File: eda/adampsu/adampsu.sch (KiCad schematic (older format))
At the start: 15 parts, among them J1 Barrel_Jack_Switch, J2 Conn_2Rows-09Pins, J3 DB9_Female, SW1 SW_Push_SPDT, U1 LM27761, U2 LT1084-5.0

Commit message: BOM completeled but using expensive LDO
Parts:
- added PC?: PlungerCap, adampsu:PlungerCap-4JWHT, symbol Custom:PlungerCap
- added Q1: BUK7880-55A_CUX, Package_TO_SOT_SMD:SOT-223-3_TabPin2, symbol Custom:BUK7880-55A_CUX
- added R3: 1k, Resistor_SMD:R_0603_1608Metric_Pad1.05x0.95mm_HandSolder, symbol Device:R
- added R4: 10k, Resistor_SMD:R_0603_1608Metric_Pad1.05x0.95mm_HandSolder, symbol Device:R
- C1, C5, C6: footprint Capacitor_SMD:C_1206_3216Metric_Pad1.42x1.75mm_HandSolder -> Capacitor_SMD:C_0603_1608Metric_Pad1.05x0.95mm_HandSolder; symbol Device:C -> adampsu-rescue:C-Device; dk (none) -> 1276-2087-1-ND; mfr (none) -> CL10B475KQ8NQNC
- C2: symbol Device:C -> adampsu-rescue:C-Device; dk (none) -> 1276-6524-1-ND; mfr (none) -> CL10B105MO8NNWC
- C3: symbol Device:C -> adampsu-rescue:C-Device; dk (none) -> 1276-6641-1-ND; mfr (none) -> CL31B106MOHNNNE
- C4: symbol Device:C -> adampsu-rescue:C-Device; dk (none) -> 1276-2769-1-ND; mfr (none) -> CL31B226KPHNNNE
- D1: footprint Diode_SMD:D_SMB -> Diode_SMD:D_SMA-SMB_Universal_Handsoldering; symbol Diode:B240 -> adampsu-rescue:B240-Diode; dk (none) -> B240A-E3/61TGICT-ND; mfr (none) -> B240A-E3/61T
- J1: footprint Connector_BarrelJack:BarrelJack_Horizontal -> adampsu:BarrelJack_CUI_PJ-047AH_Horizontal; symbol Connector:Barrel_Jack_Switch -> adampsu-rescue:Barrel_Jack_Switch-Connector; dk (none) -> CP-047AH-ND; mfr (none) -> PJ-047AH
- J2: footprint (none) -> Connector_PinHeader_2.54mm:PinHeader_2x05_P2.54mm_Vertical; symbol Connector_Generic:Conn_2Rows-09Pins -> adampsu-rescue:Conn_2Rows-09Pins-Connector_Generic
- J3: footprint (none) -> Connector_Dsub:DSUB-9_Female_Vertical_P2.77x2.84mm_MountingHoles; symbol Connector:DB9_Female -> adampsu-rescue:DB9_Female-Connector; dk (none) -> AE10928-ND; mfr (none) -> A-DF 09 PP/Z
- R1: footprint Capacitor_SMD:C_0603_1608Metric_Pad1.05x0.95mm_HandSolder -> Resistor_SMD:R_0603_1608Metric_Pad1.05x0.95mm_HandSolder; symbol Device:R -> adampsu-rescue:R-Device; dk (none) -> 541-1.54MLCT-ND; mfr (none) -> CRCW04021M54FKED
- R2: footprint Capacitor_SMD:C_0603_1608Metric_Pad1.05x0.95mm_HandSolder -> Resistor_SMD:R_0603_1608Metric_Pad1.05x0.95mm_HandSolder; symbol Device:R -> adampsu-rescue:R-Device; dk (none) -> RMCF0603FT499KCT-ND; mfr (none) -> RMCF0603FT499K
- SW1: value SW_Push_SPDT -> 30V 300mA Latching Switch; footprint (none) -> adampsu:Switch-LC1258EENP; symbol Switch:SW_Push_SPDT -> adampsu-rescue:SW_Push_SPDT-Switch; dk (none) -> EG5886-ND; mfr (none) -> LC1258EENP
- U1: symbol Regulator_SwitchedCapacitor:LM27761 -> adampsu-rescue:LM27761-Regulator_SwitchedCapacitor; dk (none) -> 296-44379-1-ND; mfr (none) -> LM27761DSGR
- U2: symbol Regulator_Linear:LT1084-5.0 -> adampsu-rescue:LT1084-5.0-Regulator_Linear
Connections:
- net labels added: GND-F
- wire segments 35 -> 43
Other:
- note added: "12V Power in and low side switch"
- note added: "Connection to computer"
- note added: "Inductive load \nflyback diode"
- moved on the sheet: C1, C2, C3, C4, C5, C6, R1, R2

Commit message: switch to buck regulator. Need to choose parts
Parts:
- removed U2: LT1084-5.0, Package_TO_SOT_THT:TO-220-3_Vertical, symbol adampsu-rescue:LT1084-5.0-Regulator_Linear
- added C? (x2): 4.7uF, Capacitor_SMD:C_0603_1608Metric_Pad1.05x0.95mm_HandSolder, symbol adampsu-rescue:C-Device
- added C? (x2): 0.01uF, Capacitor_SMD:C_0603_1608Metric_Pad1.05x0.95mm_HandSolder, symbol adampsu-rescue:C-Device
- added C? (x2): 0.1uF, symbol Device:C
- added C? (x2): 47uF, symbol adampsu-rescue:C-Device
- added C? (x2): ?, symbol adampsu-rescue:C-Device
- added C? (x2): 2200pF, symbol Device:C
- added D?: D_Schottky, symbol Device:D_Schottky
- added L?: INDUCTOR, symbol pspice:INDUCTOR
- added R?: 665k, symbol Device:R
- added R?: 130k, symbol Device:R
- added R?: 51.1, symbol Device:R
- added R?: 10.2k, symbol Device:R
- added R?: 1.96k, symbol Device:R
- added R?: R, symbol Device:R
- added U?: TPS54531DDAR, Package_SO:TI_SO-PowerPAD-8_ThermalVias, symbol Custom:TPS54531DDAR
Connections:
- wire segments 43 -> 78
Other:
- moved on the sheet: C1, C2, C3, C4, C5, C6, D1, J2, J3, PC?, R1, R2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

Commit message: Final parts selection finished
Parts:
- removed C3: 10uF, Capacitor_SMD:C_1206_3216Metric_Pad1.42x1.75mm_HandSolder, symbol adampsu-rescue:C-Device
- removed C? (x2): ?, symbol adampsu-rescue:C-Device
- added C15: 0.01uF, Capacitor_SMD:C_0603_1608Metric_Pad1.05x0.95mm_HandSolder, symbol adampsu-rescue:C-Device
- C1, C6: footprint Capacitor_SMD:C_0603_1608Metric_Pad1.05x0.95mm_HandSolder -> Capacitor_SMD:C_1206_3216Metric_Pad1.42x1.75mm_HandSolder; dk 1276-2087-1-ND -> GRM32ER71H475KA88L; maxV (none) -> 50; mfr CL10B475KQ8NQNC -> UMK316AB7475KL-T; rating (none) -> XR7
- C10, C8: renamed from C?; dk (none) -> 399-7842-1-ND; mfr (none) -> C0603C103M5RACTU; rating (none) -> XR7
- C11: renamed from C?; footprint (none) -> Capacitor_SMD:C_0603_1608Metric_Pad1.05x0.95mm_HandSolder; dk (none) -> 399-17586-1-ND; maxV (none) -> 50; mfr (none) -> C0603C222K5RAC7411; rating (none) -> XR7
- C12: renamed from C?; value 2200pF -> 22pF; footprint (none) -> Capacitor_SMD:C_0603_1608Metric_Pad1.05x0.95mm_HandSolder; dk (none) -> 478-6204-1-ND; maxV (none) -> 50; mfr (none) -> 06035C220JAT2A; rating (none) -> XR7
- C13, C14: renamed from C?; footprint (none) -> Capacitor_SMD:C_1210_3225Metric_Pad1.42x2.65mm_HandSolder; dk (none) -> 587-5922-1-ND; maxV (none) -> 10+; mfr (none) -> LMK325B7476MM-PR; rating (none) -> XR7
- C16: renamed from C?; footprint (none) -> Capacitor_SMD:C_0603_1608Metric_Pad1.05x0.95mm_HandSolder; dk (none) -> 1276-1012-2-ND; maxV (none) -> 25; mfr (none) -> CL10F104ZB8NNNC; rating (none) -> XR7
- C2: dk 1276-6524-1-ND -> 399-11133-1-ND; maxV (none) -> 10; mfr CL10B105MO8NNWC -> C0603C105K8RACTU; rating (none) -> XR7
- C3: renamed from C?; value 4.7uF -> 100uF; footprint Capacitor_SMD:C_0603_1608Metric_Pad1.05x0.95mm_HandSolder -> Capacitor_THT:CP_Radial_D8.0mm_P3.50mm; dk 1276-2087-1-ND -> 1189-1659-1-ND; maxV (none) -> 50; mfr CL10B475KQ8NQNC -> 50YXJ100MT78X11.5; rating (none) -> XR7
- C4: value 22uF -> 4.7uF; dk 1276-2769-1-ND -> GRM32ER71H475KA88L; maxV (none) -> 50; mfr CL31B226KPHNNNE -> UMK316AB7475KL-T; rating (none) -> XR7
- C5: value 4.7uF -> 10uF; footprint Capacitor_SMD:C_0603_1608Metric_Pad1.05x0.95mm_HandSolder -> Capacitor_SMD:C_0805_2012Metric_Pad1.15x1.40mm_HandSolder; dk 1276-2087-1-ND -> 490-14381-1-ND; maxV (none) -> 10+; mfr CL10B475KQ8NQNC -> GRM21BR71A106KA73K; rating (none) -> XR7
- C7: renamed from C?; footprint Capacitor_SMD:C_0603_1608Metric_Pad1.05x0.95mm_HandSolder -> Capacitor_SMD:C_1206_3216Metric_Pad1.42x1.75mm_HandSolder; dk 1276-2087-1-ND -> GRM32ER71H475KA88L; maxV (none) -> 50; mfr CL10B475KQ8NQNC -> UMK316AB7475KL-T; rating (none) -> XR7
- C9: renamed from C?; footprint (none) -> adampsu:C_0508_1220Metric_Pad1.40x1.15mm_HandSolder; dk (none) -> 490-4346-1-ND; maxV (none) -> 25; mfr (none) -> LLL216R71E104MA01L; rating (none) -> XR7
- D1: value B240 -> D_Schottky; footprint Diode_SMD:D_SMA-SMB_Universal_Handsoldering -> Diode_SMD:D_SMC_Handsoldering; dk B240A-E3/61TGICT-ND -> 641-1126-1-ND; maxV (none) -> 40; mfr B240A-E3/61T -> CDBC540-G
- D2: renamed from D?; footprint (none) -> Diode_SMD:D_SMC_Handsoldering; dk (none) -> 641-1126-1-ND; maxV (none) -> 40; mfr (none) -> CDBC540-G
- J2: dk (none) -> 1849-1002-ND; mfr (none) -> PR20205VBDN
- L1: renamed from L?; value INDUCTOR -> 4.7uH; footprint (none) -> adampsu:L_11.5x10.3_H4.8; dk (none) -> 553-3001-1-ND; mfr (none) -> PA4342.472NLT; rating (none) -> 15.5mOhm
- R10: renamed from R?; footprint (none) -> Resistor_SMD:R_0603_1608Metric_Pad1.05x0.95mm_HandSolder; dk (none) -> 311-1.96KHRCT-ND; mfr (none) -> RC0603FR-071K96L
- R5: renamed from R?; footprint (none) -> Resistor_SMD:R_0603_1608Metric_Pad1.05x0.95mm_HandSolder; dk (none) -> 311-665KHRCT-ND; mfr (none) -> RES SMD 665K OHM 1% 1/10W 0603
- R6: renamed from R?; footprint (none) -> Resistor_SMD:R_0603_1608Metric_Pad1.05x0.95mm_HandSolder; dk (none) -> 2019-RK73B1JTTD134JCT-ND; mfr (none) -> RK73B1JTTD134J
- R7: renamed from R?; value R -> 37.4k; footprint (none) -> Resistor_SMD:R_0603_1608Metric_Pad1.05x0.95mm_HandSolder; dk (none) -> 311-37.4KHRCT-ND; mfr (none) -> RC0603FR-0737K4L
- R8: renamed from R?; footprint (none) -> Resistor_SMD:R_0603_1608Metric_Pad1.05x0.95mm_HandSolder; dk (none) -> 311-51.1HRCT-ND; mfr (none) -> RC0603FR-0751R1L
- R9: renamed from R?; footprint (none) -> Resistor_SMD:R_0603_1608Metric_Pad1.05x0.95mm_HandSolder; dk (none) -> RMCF0603FT10K2CT-ND; mfr (none) -> RMCF0603FT10K2
- U2: renamed from U?; dk (none) -> 296-40801-2-ND; mfr (none) -> TPS54531DDAR
- gave numbers to parts that had none: 1
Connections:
- net +12V: now also C4.1
- net +5V: now also C15.1
- net GND: now also C4.2, C15.2
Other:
- moved on the sheet: C1, C10, C11, C12, C13, C14, C2, C3, C5, C6, C7, C8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

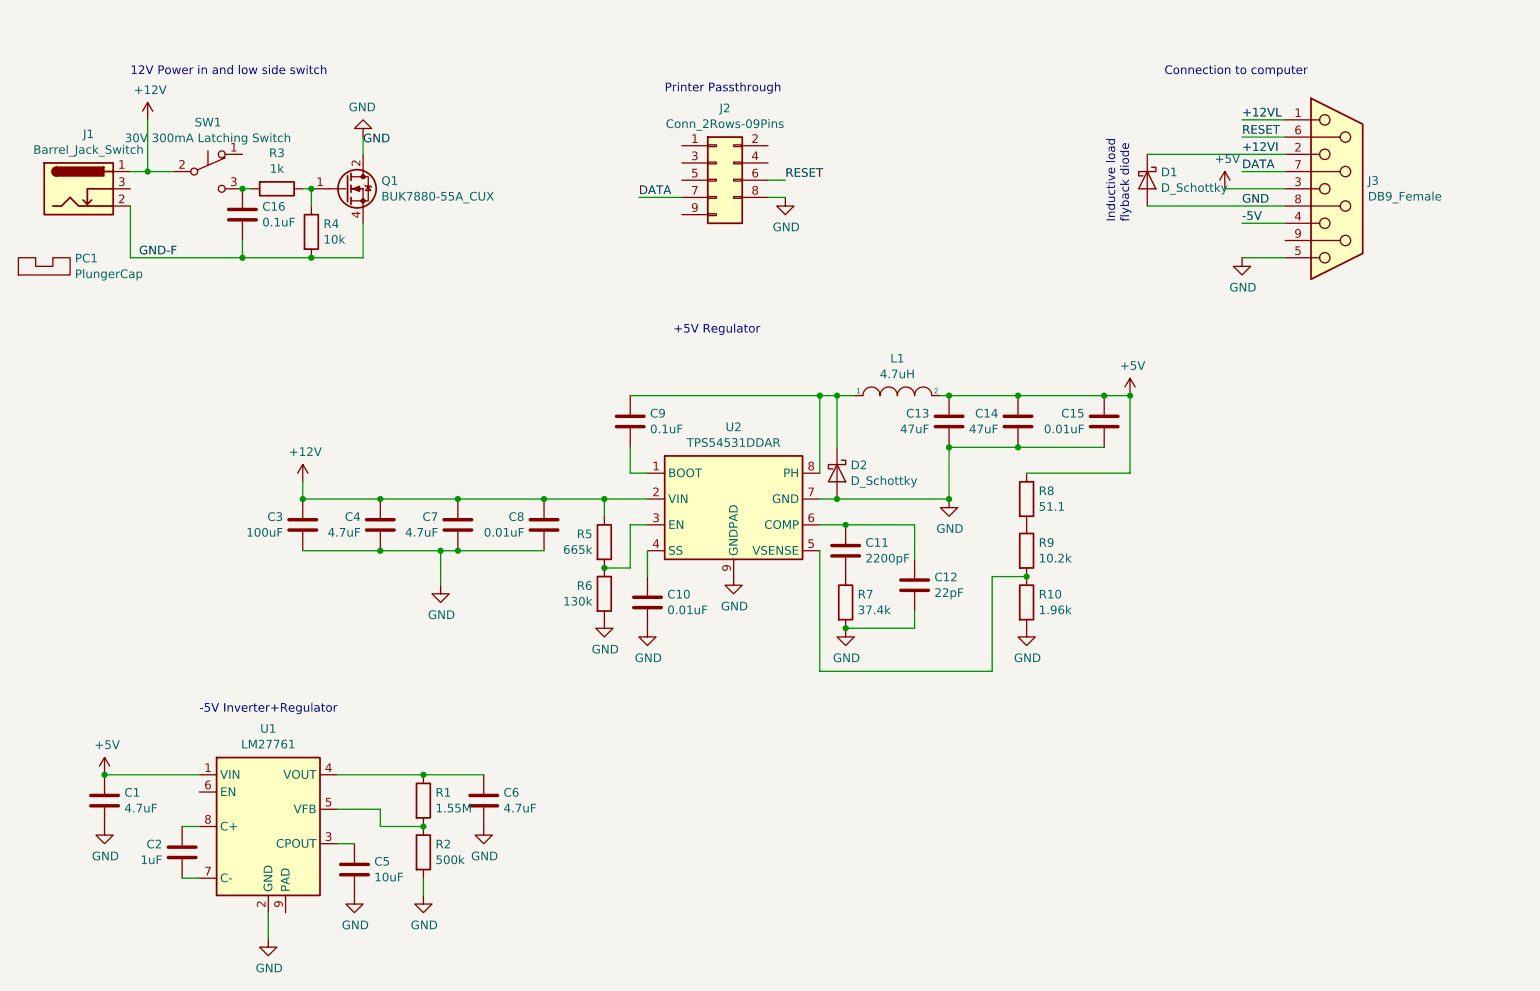
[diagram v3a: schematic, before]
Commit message: board layout started, but need new -5V regulator
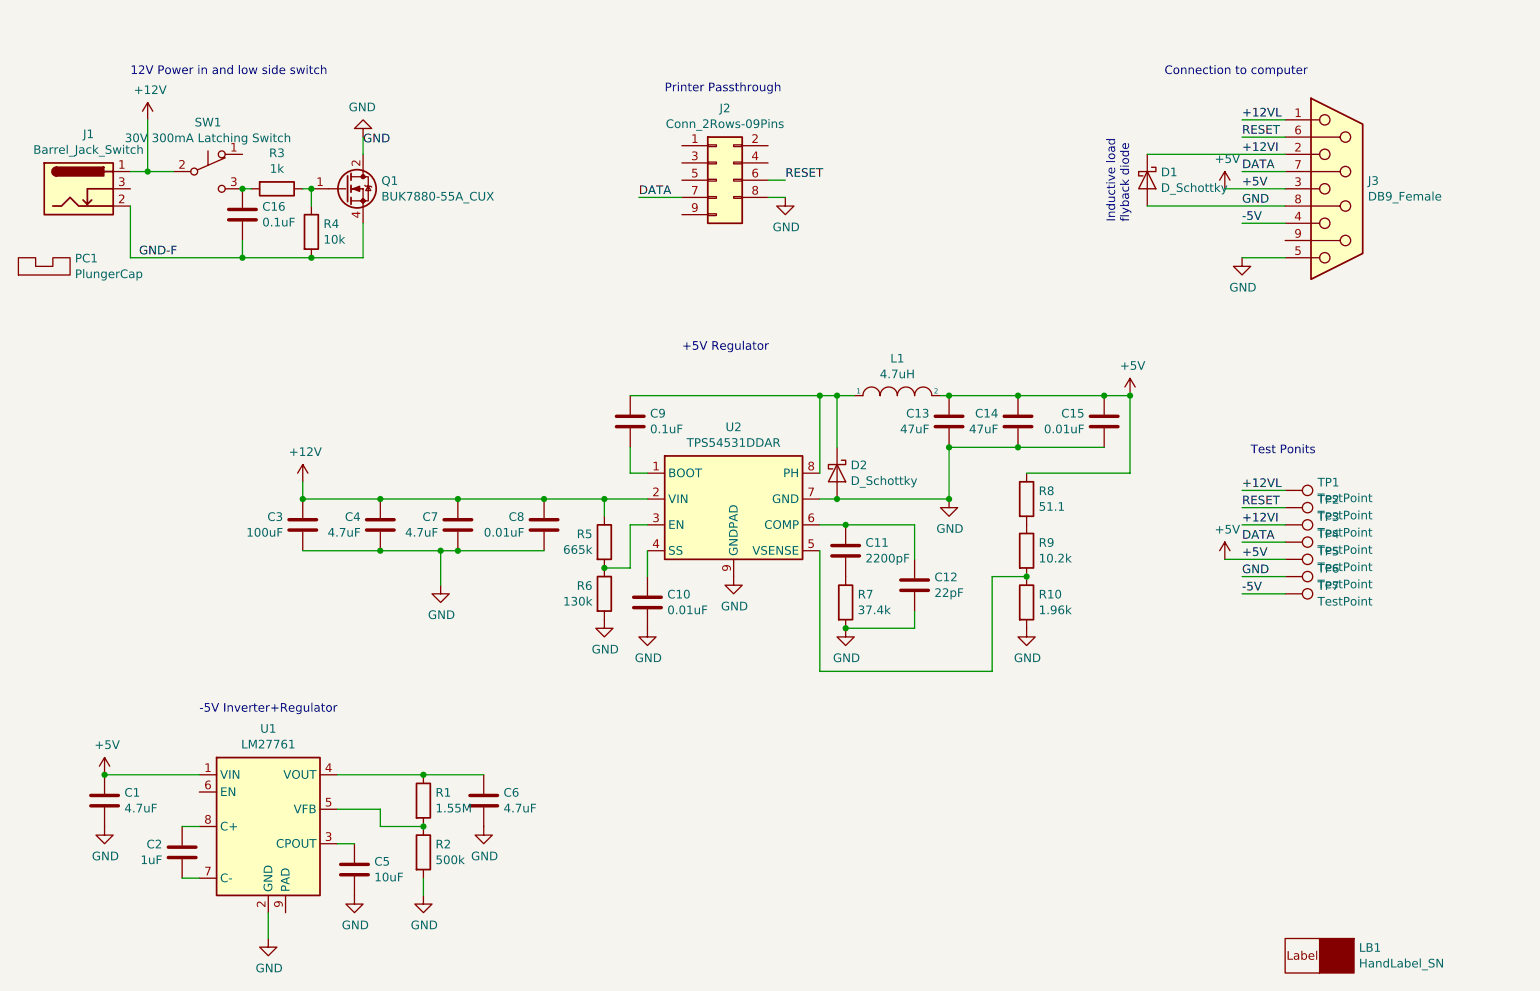
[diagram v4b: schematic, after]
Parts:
- added LB1: HandLabel_SN, adampsu:adamlabel, symbol Custom:HandLabel_SN
- added TP1, TP2, TP3, TP4, TP5, TP6, TP7: TestPoint, TestPoint:TestPoint_THTPad_2.0x2.0mm_Drill1.0mm, symbol Connector:TestPoint
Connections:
- net +12VI: now also TP3.1
- net +12VL: now also TP1.1
- net +5V: now also TP5.1
- net -5V: now also TP7.1
- net DATA: now also TP4.1
- net GND: now also TP6.1
- net RESET: now also TP2.1
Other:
- note added: "Test Ponits"
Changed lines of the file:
@@
 Wire Wire Line
 	7150 1300 7950 1300
-Text Notes 4400 2350 0    50   ~ 0
+Text Notes 4450 2450 0    50   ~ 0
 +5V Regulator
 $Comp
@@
 	6250 4300 5250 4300
 Connection ~ 6450 3750
+$Comp
+L Custom:HandLabel_SN LB1
+U 1 1 5DB90AE2
+P 8150 5950
+F 0 "LB1" H 8378 5996 50  0000 L CNN
+F 1 "HandLabel_SN" H 8378 5905 50  0000 L CNN
+F 2 "adampsu:adamlabel" H 8150 6100 50  0001 C CNN
+F 3 "" H 8150 6100 50  0001 C CNN
+	1    8150 5950
+	1    0    0    -1
+$EndComp
+$Comp
+L Connector:TestPoint TP1
+U 1 1 5DB93DBC
+P 7950 3250
+F 0 "TP1" V 7904 3438 50  0000 L CNN
+F 1 "TestPoint" V 7995 3438 50  0000 L CNN
+F 2 "TestPoint:TestPoint_THTPad_2.0x2.0mm_Drill1.0mm" H 8150 3250 50  0001 C CNN
+F 3 "~" H 8150 3250 50  0001 C CNN
+	1    7950 3250
+	0    1    1    0
+$EndComp
+Text Label 7700 1500 0    50   ~ 0
++5V
+Wire Wire Line
+	7950 3250 7700 3250
+Wire Wire Line
+	7950 3350 7700 3350
+Wire Wire Line
+	7950 3550 7700 3550
+Wire Wire Line
+	7950 3850 7700 3850
+Text Label 7700 3250 0    50   ~ 0
++12VL
+Text Label 7700 3350 0    50   ~ 0
+RESET
+Text Label 7700 3450 0    50   ~ 0
++12VI
+Text Label 7700 3550 0    50   ~ 0
+DATA
+Text Label 7700 3750 0    50   ~ 0
+GND
+Text Label 7700 3850 0    50   ~ 0
+-5V
+Wire Wire Line
+	7700 3750 7950 3750
+$Comp
+L adampsu-rescue:+5V-power #PWR0121
+U 1 1 5DBAFCDE
+P 7600 3650
+F 0 "#PWR0121" H 7600 3500 50  0001 C CNN
+F 1 "+5V" H 7615 3823 50  0000 C CNN
+F 2 "" H 7600 3650 50  0001 C CNN
+F 3 "" H 7600 3650 50  0001 C CNN
+	1    7600 3650
+	1    0    0    -1
+$EndComp
+Wire Wire Line
+	7600 3650 7950 3650
+Text Label 7700 3650 0    50   ~ 0
++5V
+$Comp
+L Connector:TestPoint TP2
+U 1 1 5DBBA2C9
+P 7950 3350
+F 0 "TP2" V 7904 3538 50  0000 L CNN
+F 1 "TestPoint" V 7995 3538 50  0000 L CNN
+F 2 "TestPoint:TestPoint_THTPad_2.0x2.0mm_Drill1.0mm" H 8150 3350 50  0001 C CNN
+F 3 "~" H 8150 3350 50  0001 C CNN
+	1    7950 3350
+	0    1    1    0
+$EndComp
+$Comp
+L Connector:TestPoint TP3
+U 1 1 5DBBA671
+P 7950 3450
+F 0 "TP3" V 7904 3638 50  0000 L CNN
+F 1 "TestPoint" V 7995 3638 50  0000 L CNN
+F 2 "TestPoint:TestPoint_THTPad_2.0x2.0mm_Drill1.0mm" H 8150 3450 50  0001 C CNN
+F 3 "~" H 8150 3450 50  0001 C CNN
+	1    7950 3450
+	0    1    1    0
+$EndComp
+$Comp
+L Connector:TestPoint TP4
+U 1 1 5DBBA974
+P 7950 3550
+F 0 "TP4" V 7904 3738 50  0000 L CNN
+F 1 "TestPoint" V 7995 3738 50  0000 L CNN
+F 2 "TestPoint:TestPoint_THTPad_2.0x2.0mm_Drill1.0mm" H 8150 3550 50  0001 C CNN
+F 3 "~" H 8150 3550 50  0001 C CNN
+	1    7950 3550
+	0    1    1    0
+$EndComp
+$Comp
+L Connector:TestPoint TP5
+U 1 1 5DBBAC81
+P 7950 3650
+F 0 "TP5" V 7904 3838 50  0000 L CNN
+F 1 "TestPoint" V 7995 3838 50  0000 L CNN
+F 2 "TestPoint:TestPoint_THTPad_2.0x2.0mm_Drill1.0mm" H 8150 3650 50  0001 C CNN
+F 3 "~" H 8150 3650 50  0001 C CNN
+	1    7950 3650
+	0    1    1    0
+$EndComp
+$Comp
+L Connector:TestPoint TP6
+U 1 1 5DBBAFC4
+P 7950 3750
+F 0 "TP6" V 7904 3938 50  0000 L CNN
+F 1 "TestPoint" V 7995 3938 50  0000 L CNN
+F 2 "TestPoint:TestPoint_THTPad_2.0x2.0mm_Drill1.0mm" H 8150 3750 50  0001 C CNN
+F 3 "~" H 8150 3750 50  0001 C CNN
+	1    7950 3750
+	0    1    1    0
+$EndComp
+$Comp
+L Connector:TestPoint TP7
+U 1 1 5DBBB3BE
+P 7950 3850
+F 0 "TP7" V 7904 4038 50  0000 L CNN
+F 1 "TestPoint" V 7995 4038 50  0000 L CNN
+F 2 "TestPoint:TestPoint_THTPad_2.0x2.0mm_Drill1.0mm" H 8150 3850 50  0001 C CNN
+F 3 "~" H 8150 3850 50  0001 C CNN
+	1    7950 3850
+	0    1    1    0
+$EndComp
+Wire Wire Line
+	7700 3450 7950 3450
+Text Notes 7750 3050 0    50   ~ 0
+Test Ponits
 $EndSCHEMATC
